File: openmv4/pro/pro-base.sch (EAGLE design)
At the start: 168 parts, among them J2 SAMTEC_FTSH-105-01-F-DVSAMTEC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, J7 MURATA_MM8130-2600RA2MURATA_M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, M1 9774030243R, M2 9774030243R, Q1 BSS138, Q2 AO3401, U1 W25Q256JVEIQ_TR, U10 STM32H743IIK6, U11 TEXAS_INSTRUMENTS_BQ24072TRGT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, U12 MICROCHIP_ATECC608A-SSHDA-BMI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, U14 IS42S32800, U2 EMIF06-MSD02N16, U3 ME6211C18M5G, U4 PAM2305AABADJ, U5 LSM6DS3TR-C, U6 MICROCHIP_USB3320C-EZK-TRMICR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, U7 LBEE5KL1DX-TEMP, U8 STMICROELECTRONICS_VL53L1CXV0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, X2 USD-1040310811, X3 DF12-36-DS, X4 S2B-PH-K-S(LF)(SN), Y0 SITIME_SIT1533AI-H4-DCC-32.76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, Y1 DSC1001BI1-024.0000

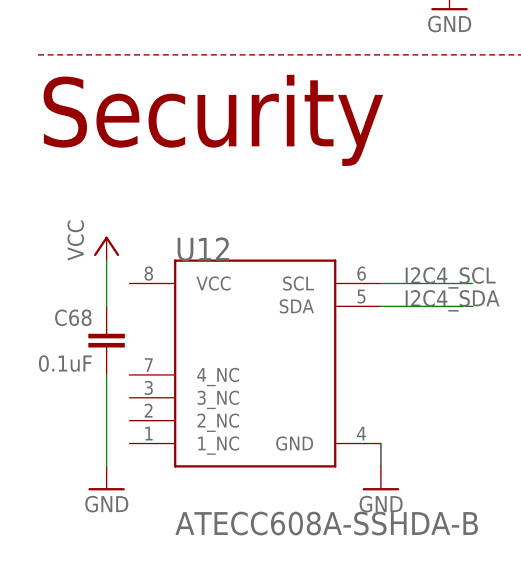
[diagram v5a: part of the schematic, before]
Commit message: Fix pin not connected to VCC
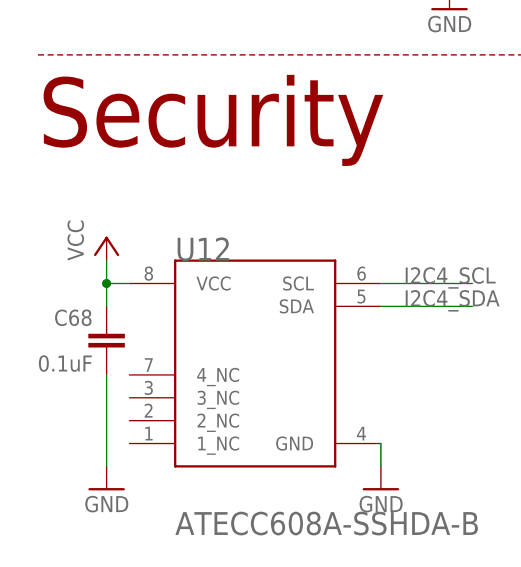
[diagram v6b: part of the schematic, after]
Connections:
- net VCC: now also U12.VCC
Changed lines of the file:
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@@
 <pinref part="C68" gate="G$1" pin="1"/>
 <pinref part="P+34" gate="VCC" pin="VCC"/>
-<wire x1="12.7" y1="320.04" x2="12.7" y2="325.12" width="0.1524" layer="91"/>
+<wire x1="12.7" y1="320.04" x2="12.7" y2="322.58" width="0.1524" layer="91"/>
+<pinref part="U12" gate="G$0" pin="VCC"/>
+<wire x1="12.7" y1="322.58" x2="12.7" y2="325.12" width="0.1524" layer="91"/>
+<wire x1="15.24" y1="322.58" x2="12.7" y2="322.58" width="0.1524" layer="91"/>
+<junction x="12.7" y="322.58"/>
 </segment>
 </net>

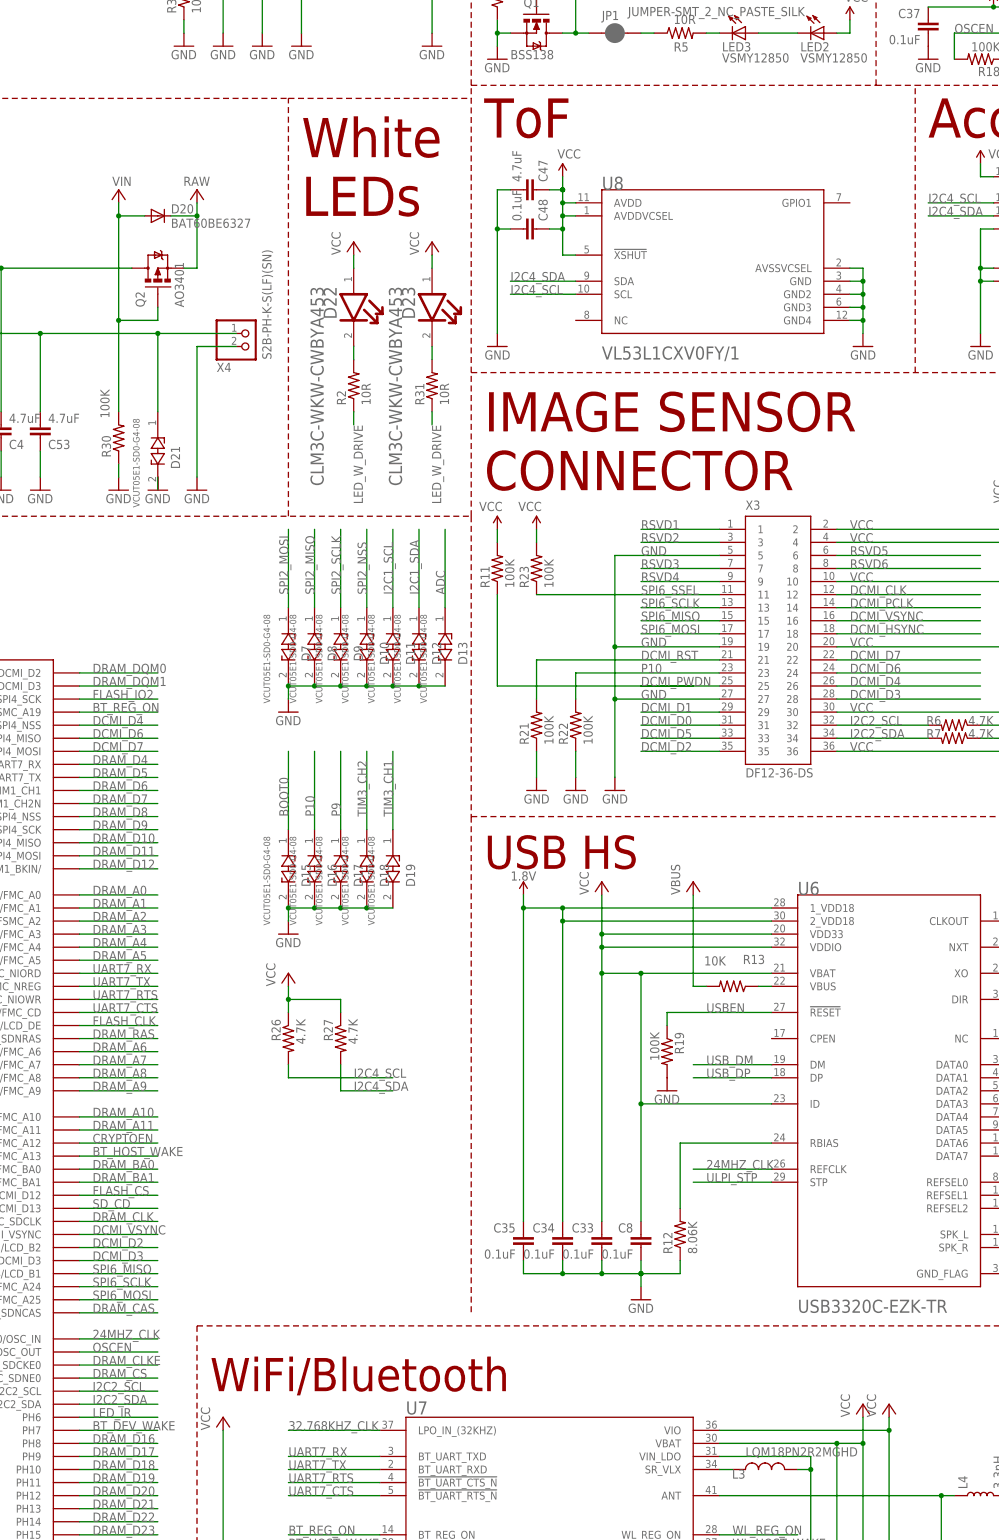
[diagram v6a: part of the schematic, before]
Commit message: Update the Pro witht he 8x8 ToF
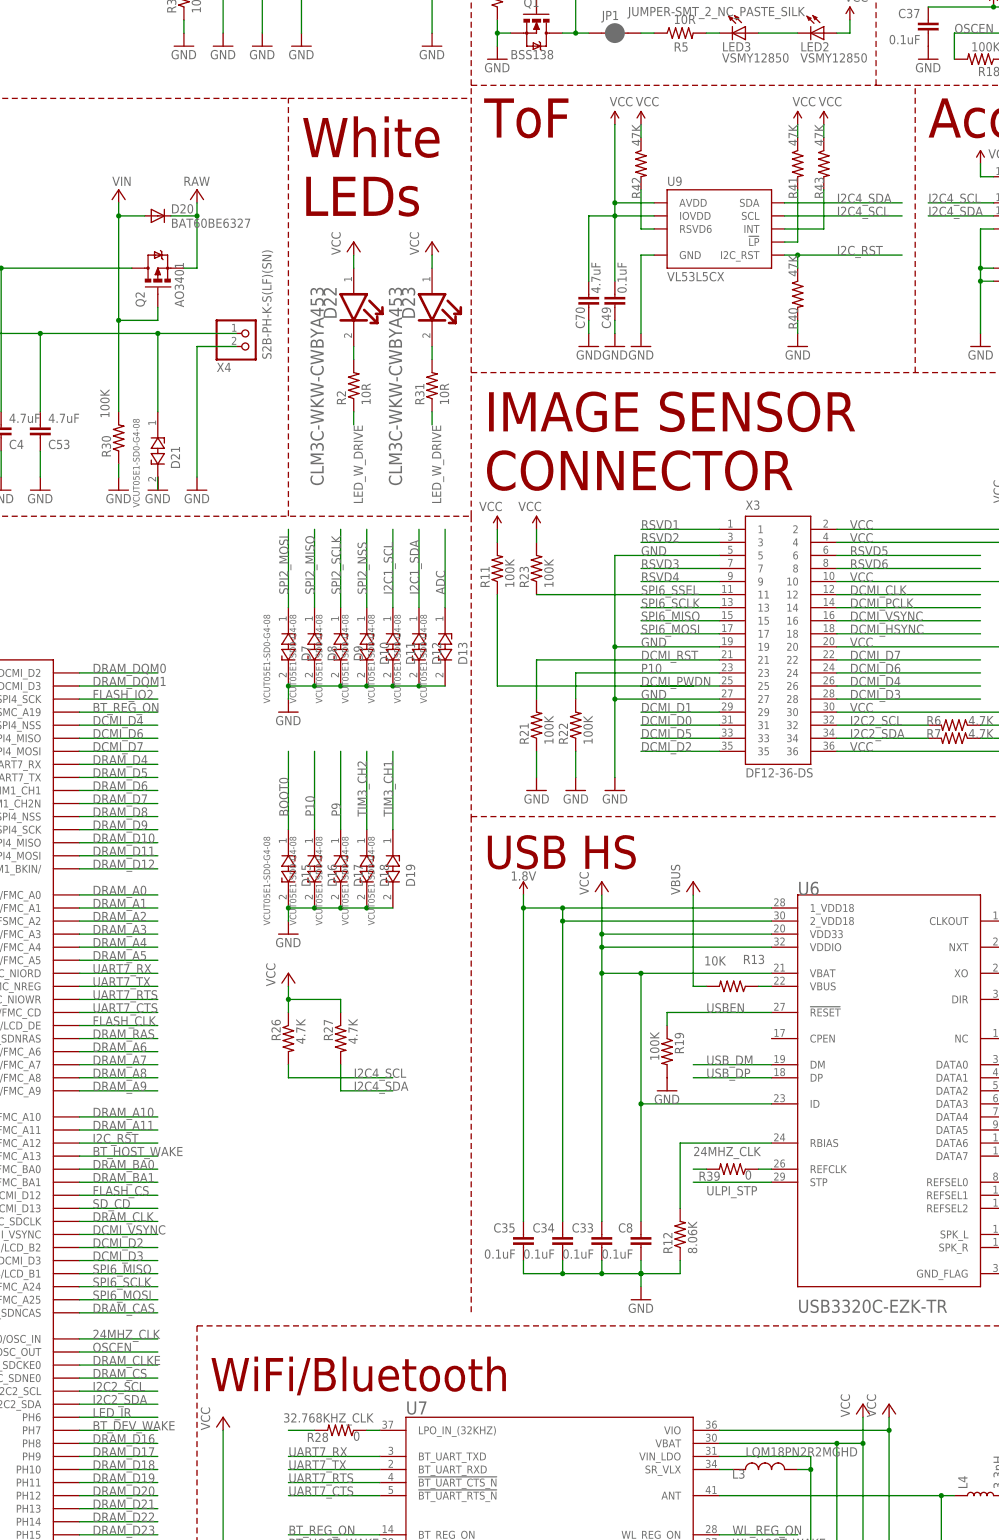
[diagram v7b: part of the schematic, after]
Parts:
- removed C47: 4.7uF, SparkFun-Capacitors:4.7UF0603
- removed C48: 0.1uF, sfe:CAP0402-CAP
- removed U8: STMICROELECTRONICS_VL53L1CXV0FY-1STMICROELECTRONICS_VL53L1C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, STMicroelectronics - VL53L1CXV0FY:STMICROELECTRONICS_VL53L1CXV0FY-1STMICROELECTRONICS_VL53L1CXV0FY-1_0_0
- added C49: 0.1uF, sfe:CAP0402-CAP
- added C70: 4.7uF, SparkFun-Capacitors:4.7UF0603
- added R28, R39: 0, sfe:RESISTOR0402-RES
- added R40, R41, R42, R43: 47K, sfe:RESISTOR0402-RES
- added U9: VL53L5CX, SparkFun-Sensors:VL53L5CX
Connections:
- removed net CRYPTOEN: U10.PG2/FMC_A12
- new net I2C_RST: R40.1, U10.PG2/FMC_A12, U9.I2C_RST
- new net N$2: R28.1, U7.LPO_IN_(32KHZ)
- new net N$3: R39.1, U6.REFCLK
- new net N$5: R41.2, U9.!LP
- new net N$6: R42.2, U9.RSVD6
- new net N$7: R43.2, U9.INT
- net 24MHZ_CLK: now also R39.2; no longer U6.REFCLK
- net 32.768KHZ_CLK: now also R28.2; no longer U7.LPO_IN_(32KHZ)
- net GND: now also C49.2, C70.1, R40.2, U9.GND; no longer C47.2, C48.2, U8.AVSSVCSEL, U8.GND, U8.GND2, U8.GND3, U8.GND4
- net I2C4_SCL: now also U9.SCL; no longer U8.SCL
- net I2C4_SDA: now also U9.SDA; no longer U8.SDA
- net VCC: now also C49.1, C70.2, R41.1, R42.1, R43.1, U9.AVDD, U9.IOVDD; no longer C47.1, C48.1, U8.!XSHUT!, U8.AVDD, U8.AVDDVCSEL

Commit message: Update pro design with fixes
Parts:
- removed ANT1: 2450AT18B100E, 2450AT18B100E:2450AT18B100E
- removed C66, C67: 1.2pf, sfe:CAP0402-CAP
- removed J7: MURATA_MM8130-2600RA2MURATA_MM8130-2600RA2_0_0, Murata - MM8130-2600RA2:MURATA_MM8130-2600RA2MURATA_MM8130-2600RA2_0_0
- removed L4: 3.3nH, SparkFun-Coils:INDUCTOR-0402-3.9NH
- added J6: RSP-122811-01, RSP-122811-01:RSP-122811-01
- added R44: 1.18K, sfe:RESISTOR0402-RES
- added R45: 46.4K, sfe:RESISTOR0402-RES
- JP2: value JUMPER-SMT_2_NC_PASTE_SILK -> JUMPER-SMT_2_NO_SILK; device SparkFun-Jumpers:JUMPER-SMT_2_NC_PASTE_SILK -> SparkFun-Jumpers:JUMPER-SMT_2_NO_SILK
- R32: value 1.8K -> 1.13K
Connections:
- net CHG_LED renamed N$10
- net P10 renamed FSIN
- removed net ANT_PI_O: C67.1, J7.IN, L4.2
- removed net N$1: ANT1.1, J7.OUT
- new net N$4: R44.2, U11.ILIM
- new net N$8: R45.1, U11.TMR
- net ANT_PI_I: now also J6.1; no longer C66.1, L4.1
- net GND: now also J6.GND, R44.1, R45.2, U11.EN1; no longer C66.2, C67.2, J7.1_GROUND, J7.2_GROUND, J7.3_GROUND, J7.4_GROUND, R19.2, U11.EN2
- net OUT: now also U11.EN2; no longer U11.EN1
- net VCC: now also R19.2
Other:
- note added: "* USBEN is pulled up to prevent USB from resetting in low power"
- note added: "Copyright (c) 2021-2023 OpenMV <openmv@openmv.io>"
- note removed: "Copyright (c) 2021 OpenMV <openmv@openmv.io>"
- moved on the sheet: D14, R33, U11
